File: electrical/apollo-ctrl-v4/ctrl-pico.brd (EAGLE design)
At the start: 88.6 x 88.9 mm, 47 parts, among them J1 ESP32-PICO-KIT, J2 DNP, J3 DNP, J4 DNP, J6 DISPLAY_RIGHT, J7 DISPLAY_LEFT, Q1 SOT23-3, U1 DNP (24LC01)

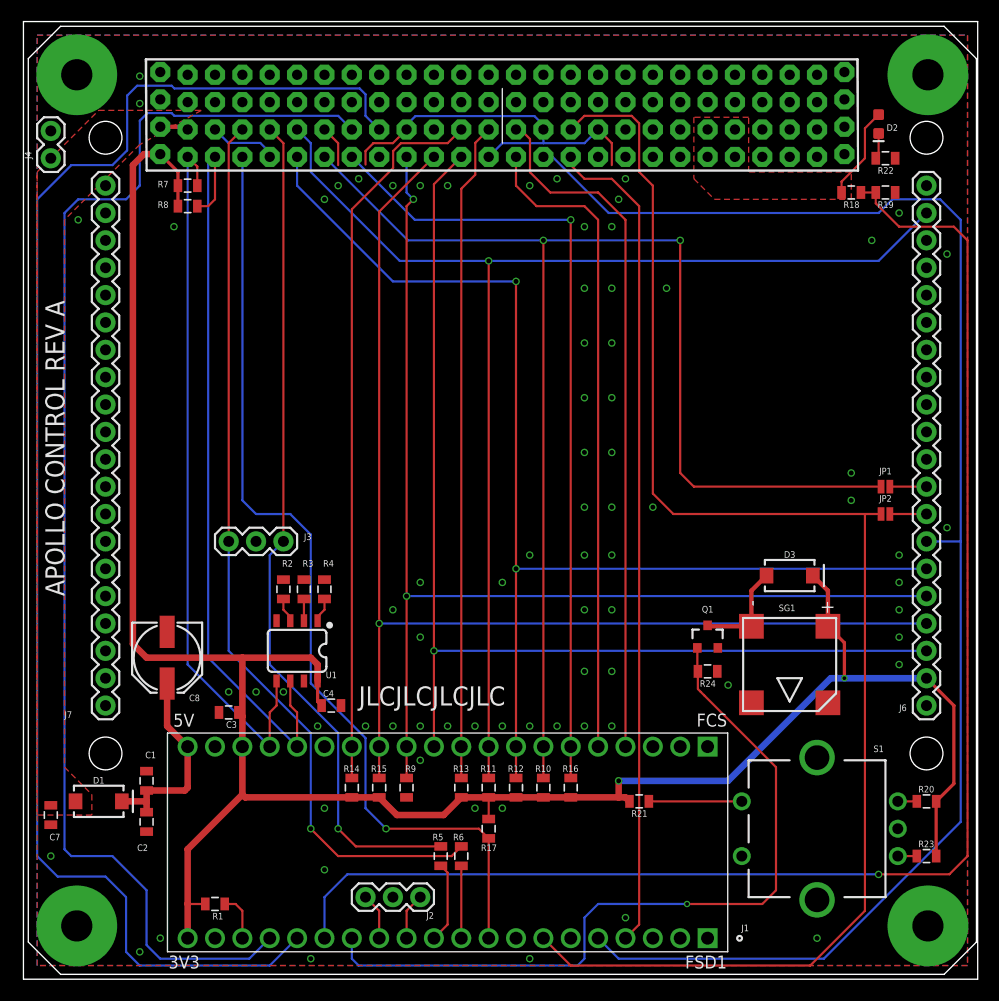
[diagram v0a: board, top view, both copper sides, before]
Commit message: Update TFT LCD pinout for version 2 of the Adafruit breakout board
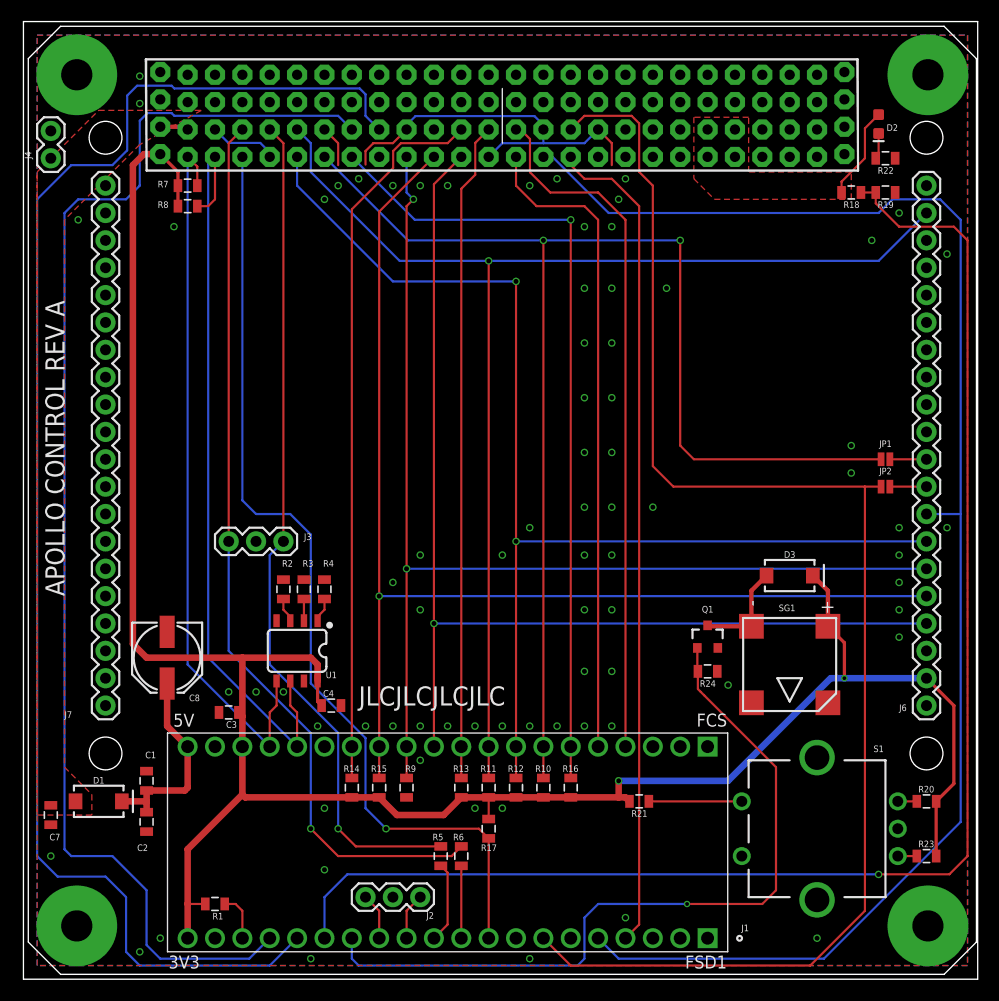
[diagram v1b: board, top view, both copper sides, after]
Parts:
- moved JP1 2.54 mm to (80.0, 48.3)
- moved JP2 2.54 mm to (80.0, 45.7)
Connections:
- net CIDO: now also J6.5; no longer J6.4
- net CODI: now also J6.6; no longer J6.5
- net CS3: now also J6.7; no longer J6.6
- net GPIO22: now also J6.8; no longer J6.7
- net LCD_BL: now also J6.10; no longer J6.9
- net LCD_RST: now also J6.9; no longer J6.8
- net SCK: now also J6.4; no longer J6.3
- net X+: now also J6.12; no longer J6.11
- net X-: now also J6.14; no longer J6.13
- net Y+: now also J6.11; no longer J6.10
- net Y-: now also J6.13; no longer J6.12
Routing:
- net CS5: track 126.9 -> 124.3 mm

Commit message: Add touch screen connectors on control PCB, and roll up fab to B
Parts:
- moved R10 1.78 mm to (48.3, 16.0), turned to 90 degrees
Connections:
- removed net CS5: J1.J3_7, JP1.1, R10.1, U$1.P$25
- removed net SCL2: J1.J2_6
- removed net SDA2: J1.J2_8
- removed net X+: J6.12
- removed net X-: J6.14
- removed net Y+: J6.11
- removed net Y-: J6.13
- new net ADC5: J1.J2_15, J6.11
- new net BUZ: J1.J2_6, Q1.1, R24.2
- new net LCD_CD: J1.J2_8, J6.8, R10.1
- net ADC2: now also J1.J3_7, J6.12; no longer J1.J2_14, Q1.1, R24.2
- net ADC3: now also J6.14; no longer U$1.P$30
- net ADC4: now also J6.13; no longer U$1.P$34
- net GPIO22: now also JP1.1; no longer J6.8
- net VMON: now also J1.J2_14; no longer J1.J2_15
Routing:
- net CS5: track 124.3 -> 0.00 mm, vias 2 -> 0
- net ADC5: track 0.00 -> 110.6 mm
- net LCD_CD: track 0.00 -> 75.5 mm, vias 0 -> 3
- net BUZ: track 0.00 -> 36.3 mm, vias 0 -> 1
- net ADC4: track 135.3 -> 116.3 mm
- net GPIO22: track 141.0 -> 152.3 mm, vias 0 -> 1
- net ADC2: track 72.2 -> 67.3 mm
- net ADC3: track 120.7 -> 119.8 mm
- net +3V3: track 207.7 -> 206.9 mm
- net !FAULT!: track 88.9 -> 89.6 mm
- net VMON: track 134.6 -> 134.0 mm
- net GND: vias 77 -> 84
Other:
- board text added: "APOLLO CONTROL REV B"
- board text removed: "APOLLO CONTROL REV A"
